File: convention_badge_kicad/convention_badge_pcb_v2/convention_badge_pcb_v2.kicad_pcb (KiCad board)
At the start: 4 copper layers, 90 x 98 mm, 48 parts, among them J1 USBC, J2 Conn_01x03_Pin, J3 3.7V Battery, J4 Conn_01x07_Pin, J5 Conn_01x07_Pin, Q1 LP0404N3T5G, SW1 SW4X2, SW2 SW4X2, SW3 SW_Push, SW4 SW_Push, SW5 SW_Push, SW6 SW4X2, U1 ESP32-C3-WROOM-02, U2 FS8205A, U3 TP4056, U4 DW01A, U5 TLV75733PDBV

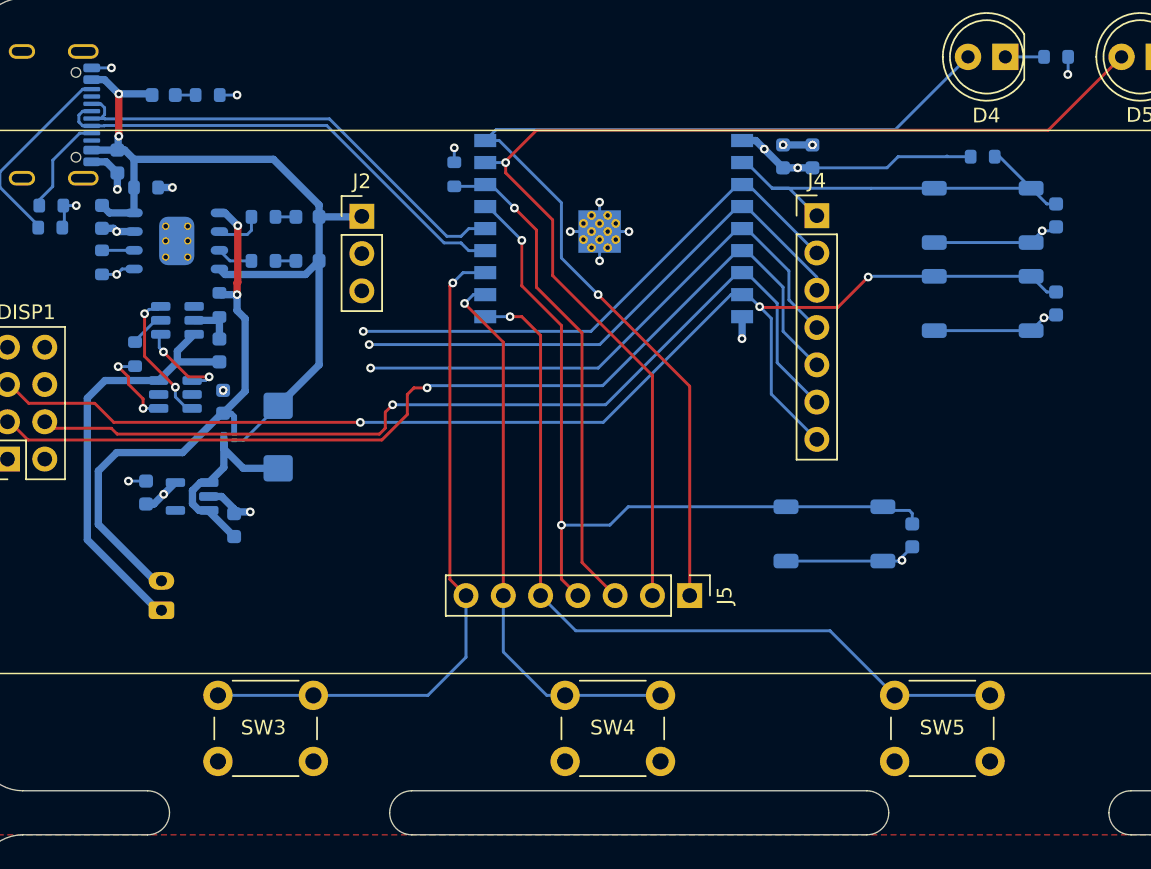
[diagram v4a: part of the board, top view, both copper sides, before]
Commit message: updated with part numbers and modified board to account for avail parts
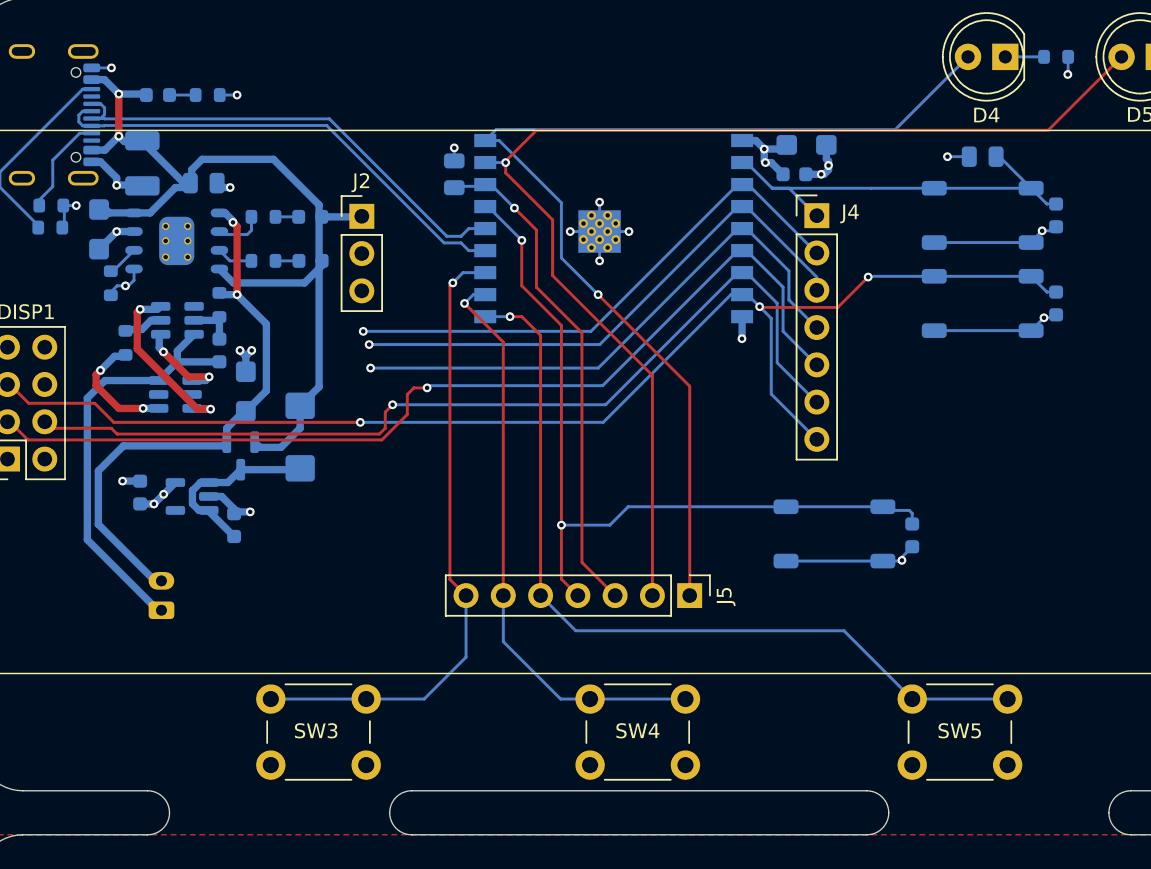
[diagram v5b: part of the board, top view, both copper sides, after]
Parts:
- C1: value 1uf -> 1uF; footprint PCM_JLCPCB:C_0603 -> Capacitor_SMD:C_0603_1608Metric
- C10: footprint PCM_JLCPCB:C_0603 -> PCM_JLCPCB:C_CASE-A-3216-18(mm)
- C11, C2: value 0.1uf -> 0.1uF; footprint PCM_JLCPCB:C_0603 -> Capacitor_SMD:C_0603_1608Metric
- C3, C4: value 10uf -> 10uF; footprint PCM_JLCPCB:C_0603 -> PCM_JLCPCB:C_CASE-A-3216-18(mm)
- C5, C6, C8, C9: footprint PCM_JLCPCB:C_0603 -> Capacitor_SMD:C_0603_1608Metric
- C7: footprint PCM_JLCPCB:C_0603 -> PCM_JLCPCB:C_CASE-B-3528-21(mm)
- D1: value LED -> YEL_LED
- D2, D7: value LED -> RED_LED
- Q1: value LP0404N3T5G -> AO3401A; footprint Package_TO_SOT_SMD:SOT-883 -> Package_TO_SOT_SMD:SOT-23
- R10, R3, R4: footprint PCM_JLCPCB:R_0603 -> Resistor_SMD:R_0805_2012Metric
- moved R10 3.94 mm to (124.9, 85.6)
- moved SW3 3.61 mm to (129.5, 120.8)
- moved C10 1.78 mm to (166.0, 83.0), turned to 0 degrees
- moved C9 1.73 mm to (165.2, 85.0), turned to 0 degrees
- moved SW4 1.72 mm to (151.2, 120.8)
- moved C7 1.71 mm to (120.8, 84.2)
- moved C4 1.70 mm to (127.8, 99.8)
- moved R7 1.54 mm to (118.6, 92.4)
- moved Q1 1.52 mm to (127.5, 104.2), turned to -90 degrees
- moved D3 1.50 mm to (131.5, 102.9)
- moved SW5 1.23 mm to (173.2, 120.8)
- moved R9 1.00 mm to (119.6, 96.5)
- moved C3 0.87 mm to (117.8, 88.8)
- moved C8 0.40 mm to (120.6, 106.7)
- moved D7 0.39 mm to (121.8, 79.6)
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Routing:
- net +3.3V: track 20.6 -> 11.4 mm, vias 4 -> 6
- net GND: track 58.8 -> 65.1 mm, vias 22 -> 23
- net /VUSB: track 60.8 -> 64.8 mm
- net /GPIO21: track 46.5 -> 43.0 mm
- net Net-(U2-G1): track 9.31 -> 12.2 mm
- net Net-(U2-S1): track 5.78 -> 8.17 mm
- net Net-(D3-K): track 14.7 -> 12.7 mm
- net /GPIO20: track 38.7 -> 40.1 mm
- net /GPIO10: track 55.5 -> 56.8 mm
- net /VBAT: track 38.1 -> 39.1 mm

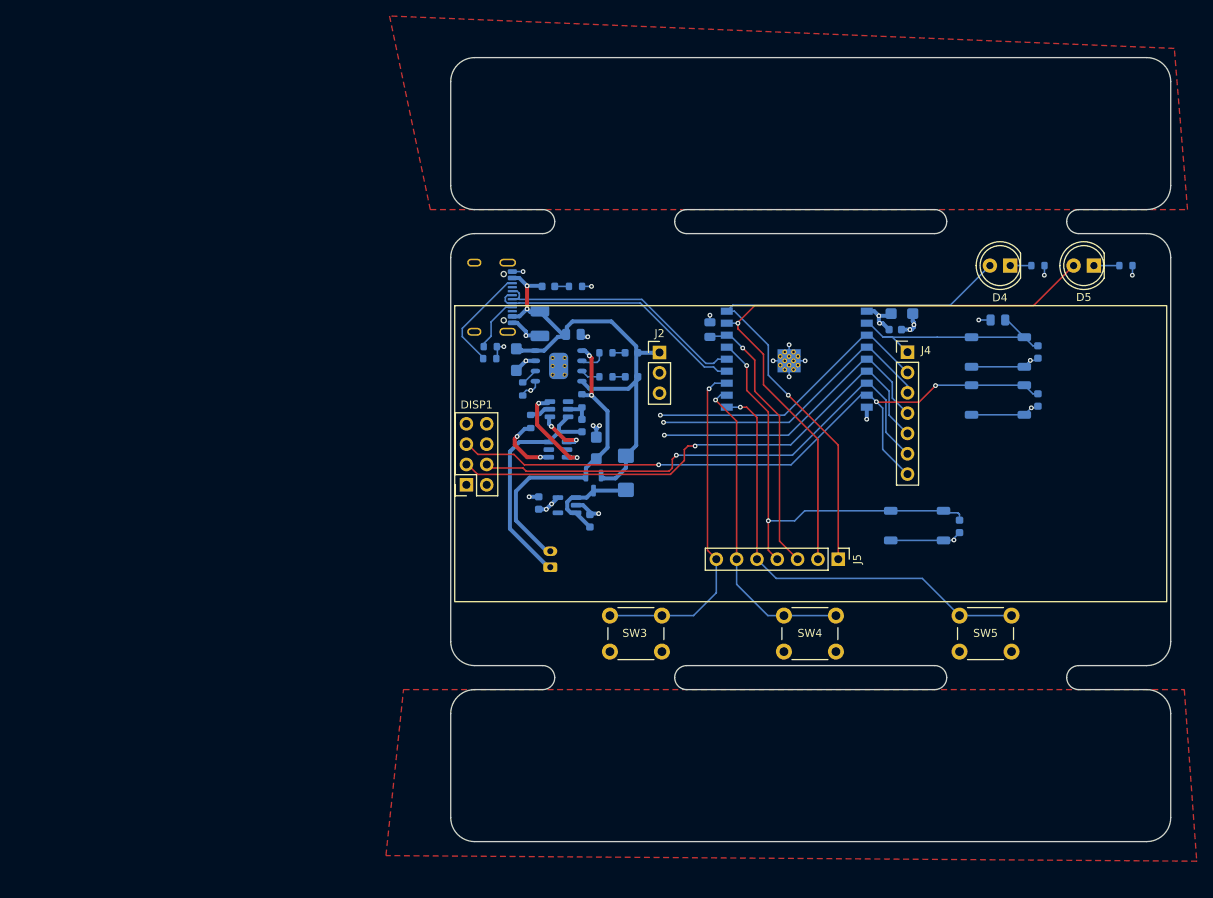
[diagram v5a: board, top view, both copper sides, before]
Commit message: added solar pannel design, almost ready to order
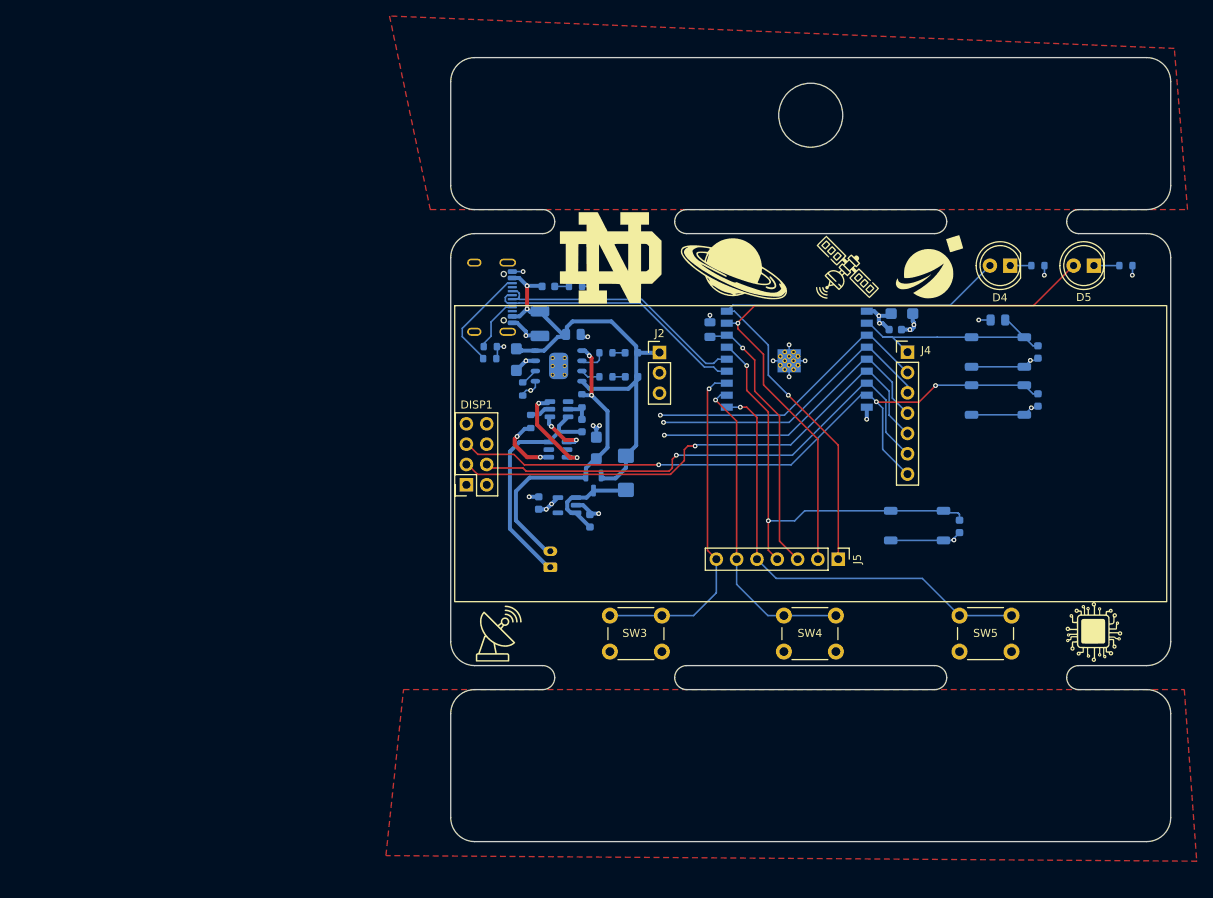
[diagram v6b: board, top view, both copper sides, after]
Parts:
- added G***: LOGO, LOGO, F.Cu at (115.6, 123.0)
- added G***: LOGO, LOGO, F.Cu at (129.6, 76.0)
- added G***: LOGO, LOGO, F.Cu at (145.0, 77.4)
- added G***: LOGO, LOGO, F.Cu at (169.6, 77.0)
- added G***: LOGO, LOGO, F.Cu at (155.0, 61.6)
- added G***: LOGO, LOGO, F.Cu at (190.0, 122.8)
- added G***: LOGO, LOGO, F.Cu at (159.2, 77.2)
- added G***: LOGO, LOGO, F.Cu at (155.0, 140.4)
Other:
- outline, holes or cut-outs redrawn
- board text added: "0"
- board text added: "1"
- board text added: "10"
- board text added: "2"
- board text added: "20"
- board text added: "21"
- board text added: "3"
- board text added: "3.3V"
- board text added: "4"
- board text added: "5"
- board text added: "5V"
- board text added: "6"
- board text added: "7"
- board text added: "8"
- board text added: "9"
- board text added: "CHRG"
- board text added: "Convention PCB Badge V2"
- board text added: "GND"
- board text added: "STDBY"
- board text added: "WAKE"

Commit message: submitted to jlcpcb
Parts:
- moved G*** 0.28 mm to (190.2, 123.0)
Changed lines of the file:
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@@
 		(allow_soldermask_bridges_in_footprints no)
 		(tenting front back)
+		(aux_axis_origin 109.6 149)
+		(grid_origin 109.6 149)
 		(pcbplotparams
 			(layerselection 0x00000000_00000000_55555555_575555ff)
@@
 	(footprint "LOGO"
 		(layer "F.Cu")
-		(at 190 122.8)
+		(at 190.2 123)
 		(property "Reference" "G***"
 			(at 0 0 0)
@@
 			)
 		)
+		(property "LCSC" "C2337"
+			(at 0 0 0)
+			(unlocked yes)
+			(layer "F.Fab")
+			(hide yes)
+			(effects
+				(font
+					(size 1 1)
+					(thickness 0.15)
+				)
+			)
+		)
 		(property ki_fp_filters "Connector*:*_1x??_*")
 		(sheetname "/")
@@
 			)
 		)
+		(property "LCSC" ""
+			(at 0 0 0)
+			(unlocked yes)
+			(layer "F.Fab")
+			(hide yes)
+			(effects
+				(font
+					(size 1 1)
+					(thickness 0.15)
+				)
+			)
+		)
 		(property ki_fp_filters "Connector*:*_1x??_*")
 		(sheetname "/")
@@
 			)
 		)
+		(property "LCSC" ""
+			(at 0 0 270)
+			(unlocked yes)
+			(layer "F.Fab")
+			(hide yes)
+			(effects
+				(font
+					(size 1 1)
+					(thickness 0.15)
+				)
+			)
+		)
 		(property ki_fp_filters "Connector*:*_1x??_*")
 		(sheetname "/")
@@
 			)
 		)
-		(property "LCSC" " C318884"
+		(property "LCSC" "C318884"
 			(at 0 0 0)
 			(unlocked yes)
@@
 			)
 		)
-		(property "LCSC" "C1590"
+		(property "LCSC" "C14663"
 			(at 0 0 0)
 			(unlocked yes)
@@
 			)
 		)
-		(property "LCSC" " C485517"
+		(property "LCSC" "C485517"
 			(at 0 0 180)
 			(unlocked yes)
@@
 			)
 		)
-		(property "LCSC" "C1590"
+		(property "LCSC" "C14663"
 			(at 0 0 270)
 			(unlocked yes)
@@
 			)
 		)
-		(property "LCSC" "C2287"
+		(property "LCSC" "C2290"
 			(at 0 0 0)
 			(unlocked yes)
@@
 			)
 		)
-		(property "LCSC" " C351410"
+		(property "LCSC" "C351410"
 			(at 0 0 0)
 			(unlocked yes)
@@
 			)
 		)
-		(property "LCSC" " C318884"
+		(property "LCSC" "C318884"
 			(at 0 0 0)
 			(unlocked yes)
@@
 			)
 		)
-		(property "LCSC" "C1590"
+		(property "LCSC" "C14663"
 			(at 0 0 270)
 			(unlocked yes)
@@
 			)
 		)
-		(property "LCSC" "C1607"
+		(property "LCSC" "C23630"
 			(at 0 0 90)
 			(unlocked yes)
@@
 			)
 		)
-		(property "LCSC" "C1607"
+		(property "LCSC" "C23630"
 			(at 0 0 90)
 			(unlocked yes)
@@
 			)
 		)
-		(property "LCSC" "C1590"
+		(property "LCSC" "C14663"
 			(at 0 0 270)
 			(unlocked yes)
@@
 			)
 		)
-		(property "LCSC" " C318884"
+		(property "LCSC" "C318884"
 			(at 0 0 0)
 			(unlocked yes)
